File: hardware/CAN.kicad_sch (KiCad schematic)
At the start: 0 parts

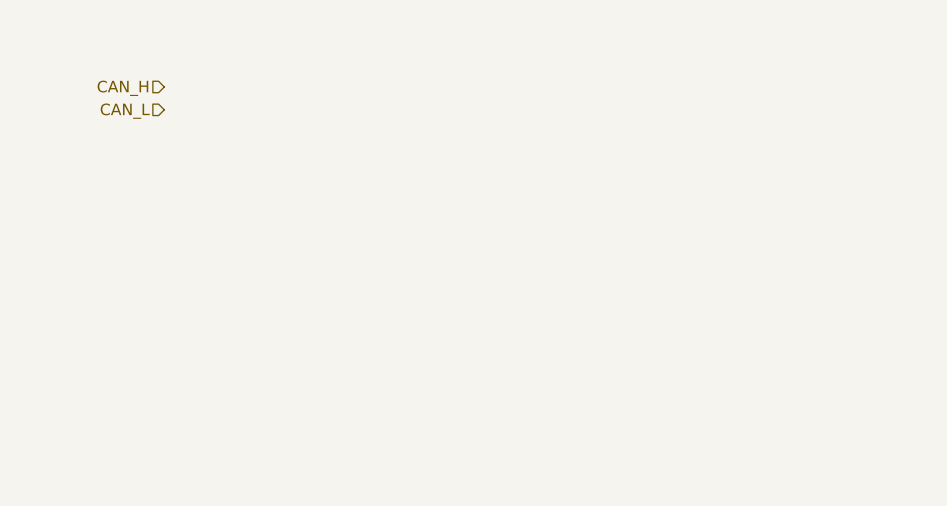
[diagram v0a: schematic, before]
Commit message: Schematic updates: stm32 sheet
Signed-off-by: Connor Rigby <connorr@hey.com>
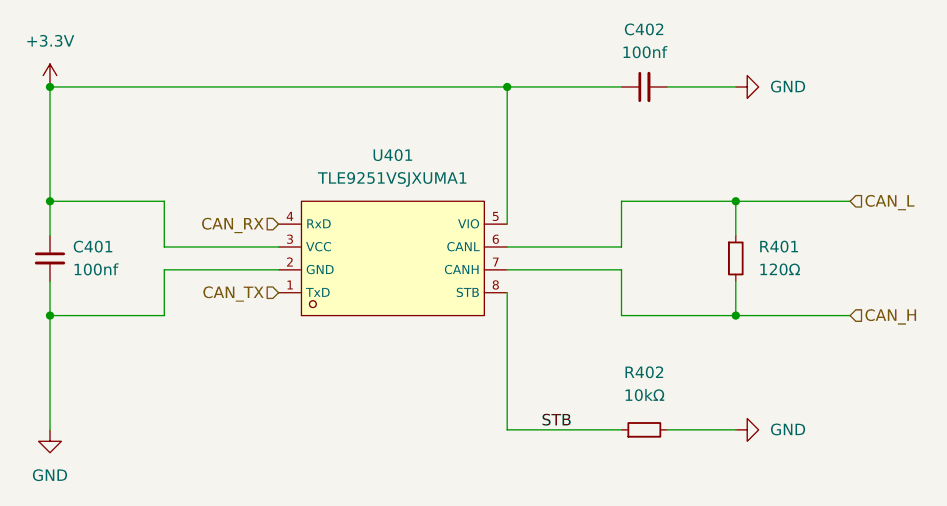
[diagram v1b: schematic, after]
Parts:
- added C401, C402: C_0402_100nf_X7R, Capacitor_SMD:C_0402_1005Metric, symbol LCSC_Capacitor:C_0402_100nf_X7R
- added R401: R_1206_120, Resistor_SMD:R_1206_3216Metric, symbol LCSC_Resistor:R_1206_120
- added R402: R_0402_10k, Resistor_SMD:R_0402_1005Metric, symbol LCSC_Resistor:R_0402_10k
- added U401: TLE9251VSJXUMA1, Package_SO:Infineon_PG-DSO-8-43, symbol LCSC_Communication_Interface_Chip_UART_485_232:TLE9251VSJXUMA1
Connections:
- net CAN_H: now also R401.2, U401.7 (CANH)
- net CAN_L: now also R401.1, U401.6 (CANL)
- new net +3.3V: C401.1, C402.1, U401.3 (VCC), U401.5 (VIO)
- new net CAN_RX: U401.4 (RxD)
- new net CAN_TX: U401.1 (TxD)
- new net GND: C401.2, C402.2, R402.2, U401.2 (GND)
- new net STB: R402.1, U401.8 (STB)

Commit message: Pre-production updates
Signed-off-by: Connor Rigby <connorr@hey.com>
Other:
- company: (none) -> https://cone.codes
- title: (none) -> coneRGB2
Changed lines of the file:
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@@
 (kicad_sch (version 20230121) (generator eeschema)
   (paper "A4")
+  (title_block
+    (title "coneRGB2")
+    (date "2023-03-20")
+    (rev "1")
+    (company "https://cone.codes")
+    (comment 1 "https://github.com/connorrigby/underglow2")
+    (comment 2 "Designed by Connor Rigby")
+    (comment 3 "Handles CAN TX/RX => H/L differential signaling")
+    (comment 4 "CAN Transciever")
+  )
   (junction (at 25.4 25.4) (diameter 0) (color 0 0 0 0)
   )
@@
     (stroke (width 0) (type default))
   )
+  (text_box "TODO: Consider ESD protection"
+    (at 38.1 55.88 0) (size 33.02 3.81)
+    (stroke (width 0) (type default))
+    (fill (type none))
+    (effects (font (size 1.27 1.27)) (justify left top))
+  )
   (label "STB" (at 80.01 63.5 0) (fields_autoplaced)

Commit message: Rev 2 submitted for production
Signed-off-by: Connor Rigby <connorr@hey.com>
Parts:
- U401: footprint Package_SO:Infineon_PG-DSO-8-43 -> Package_SO:SOIC-8_3.9x4.9mm_P1.27mm
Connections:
- net +3.3V renamed VDD
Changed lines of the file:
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@@
   (title_block
     (title "coneRGB2")
-    (date "2023-03-20")
-    (rev "1")
+    (date "2023-05-04")
+    (rev "2")
     (company "https://cone.codes")
     (comment 1 "https://github.com/connorrigby/underglow2")
@@
       (effects (font (size 1.27 1.27)))
     )
-    (property "Footprint" "Package_SO:Infineon_PG-DSO-8-43" (at 69.85 44.45 0)
+    (property "Footprint" "Package_SO:SOIC-8_3.9x4.9mm_P1.27mm" (at 69.85 44.45 0)
       (effects (font (size 1.27 1.27) italic) hide)
     )
@@
     (pin "3")
     (pin "4")
-    (pin "5")
     (pin "6")
     (pin "7")
     (pin "8")
+    (pin "5")
     (instances
       (project "underglow2"
@@
     )
   )
-  (symbol (lib_id "power:+3.3V") (at 25.4 25.4 0) (unit 1)
-    (in_bom yes) (on_board yes) (dnp no) (fields_autoplaced)
-    (property "Reference" "#PWR0123" (at 25.4 29.21 0)
-      (effects (font (size 1.27 1.27)) hide)
-    )
-    (property "Value" "+3.3V" (at 25.4 20.32 0)
+  (symbol (lib_id "power:VDD") (at 25.4 25.4 0) (unit 1)
+    (in_bom yes) (on_board yes) (dnp no) (fields_autoplaced)
+    (property "Reference" "#PWR0111" (at 25.4 29.21 0)
+      (effects (font (size 1.27 1.27)) hide)
+    )
+    (property "Value" "VDD" (at 25.4 21.59 0)
       (effects (font (size 1.27 1.27)))
     )
@@
       (project "underglow2"
         (path "/dcbdf88a-d6ac-4b1d-9514-0b0ce113d90b/d5721a02-112a-4ac6-b068-821a8e1fc3da"
-          (reference "#PWR0123") (unit 1)
-        )
-      )
+          (reference "#PWR0111") (unit 1)
+        )
+      )
